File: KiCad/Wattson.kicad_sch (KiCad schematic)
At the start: 15 parts, among them J1 DC, J2 USB A, J3 Banana/Spade, J4 Banana/Spade, J5 USB A, J6 Spade/Banana/Alligator, J7 Spade/Banana/Alligator, M1 24V, SW1 Power On, U1 Power Monitor VIN, U2 Power Monitor VADJ, U3 LM317 Regulator (VADJ 4V5-40V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

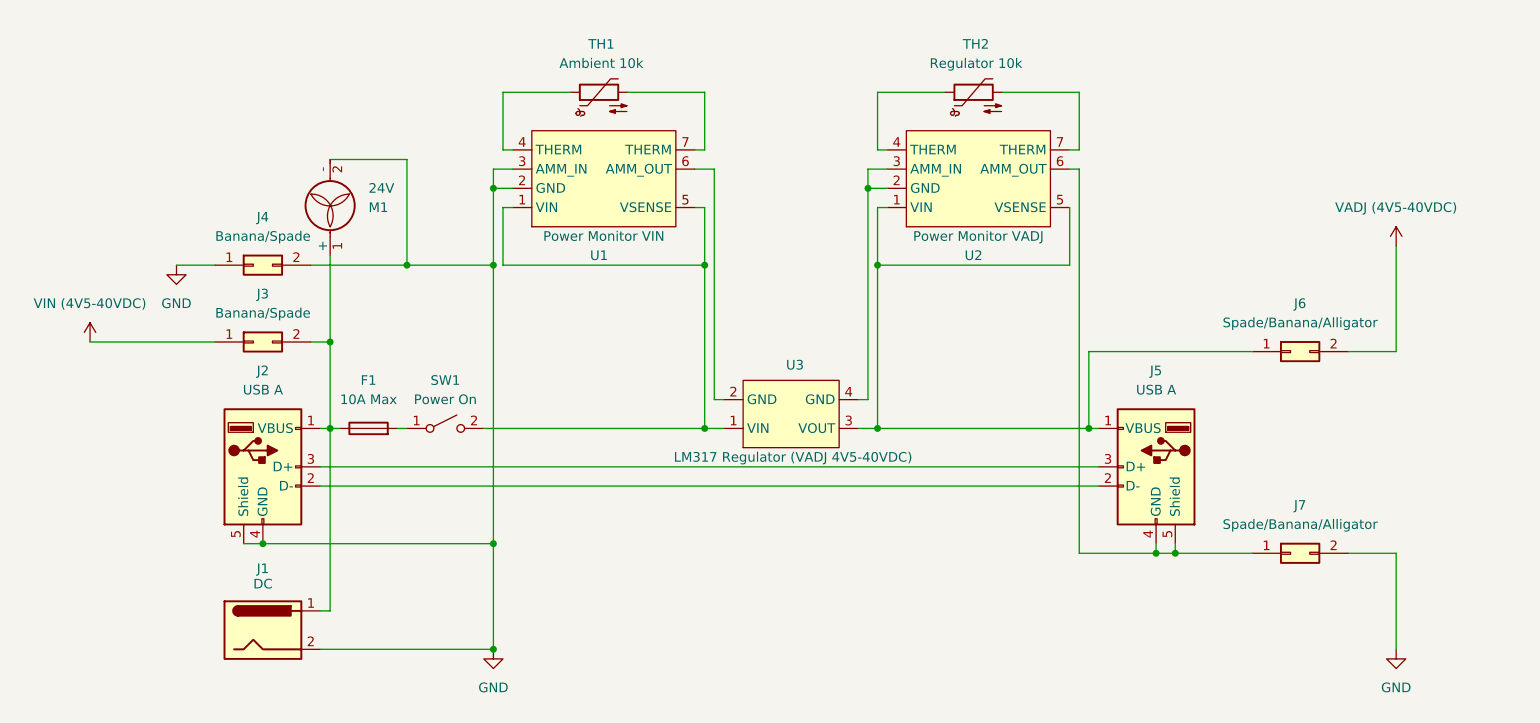
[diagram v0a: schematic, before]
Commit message: Vbus blocking diode
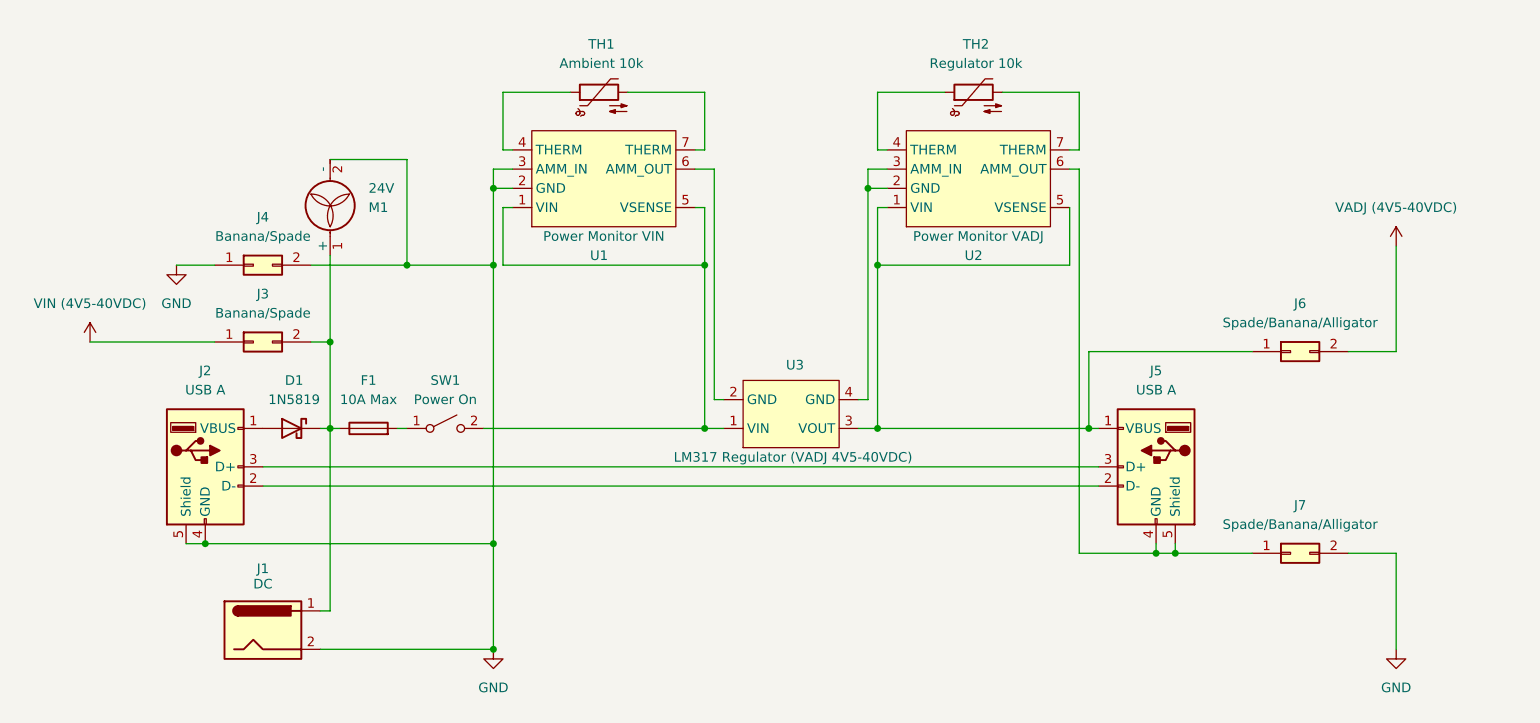
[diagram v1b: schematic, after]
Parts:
- added D1: 1N5819, Diode_THT:D_DO-41_SOD81_P10.16mm_Horizontal, symbol Diode:1N5819
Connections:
- net at F1.1, J1.1, J3.2 (Pin_2)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: now also D1.1 (K); no longer J2.1 (VBUS)
- new net: D1.2 (A), J2.1 (VBUS)
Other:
- moved on the sheet: J2
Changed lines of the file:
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@@
 	(title_block
 		(title "Wattson")
-		(date "2025-04-20")
-		(rev "1")
+		(date "2025-09-02")
+		(rev "1.1")
 		(company "Illusion Interactive")
 	)
@@
 	)
 	(junction
+		(at 60.96 125.73)
+		(diameter 0)
+		(color 0 0 0 0)
+	)
+	(junction
 		(at 99.06 139.7)
 		(diameter 0)
@@
 	)
 	(junction
-		(at 68.58 125.73)
-		(diameter 0)
-		(color 0 0 0 0)
-	)
-	(junction
 		(at 99.06 125.73)
 		(diameter 0)
@@
 	(wire
 		(pts
+			(xy 58.42 125.73) (xy 60.96 125.73)
+		)
+		(stroke
+			(width 0)
+			(type default)
+		)
+	)
+	(wire
+		(pts
 			(xy 148.59 78.74) (xy 151.13 78.74)
 		)
@@
 	(wire
 		(pts
-			(xy 68.58 125.73) (xy 99.06 125.73)
-		)
-		(stroke
-			(width 0)
-			(type default)
-		)
-	)
-	(wire
-		(pts
 			(xy 149.86 73.66) (xy 149.86 66.04)
 		)
@@
 	(wire
 		(pts
+			(xy 60.96 125.73) (xy 99.06 125.73)
+		)
+		(stroke
+			(width 0)
+			(type default)
+		)
+	)
+	(wire
+		(pts
 			(xy 77.47 74.93) (xy 87.63 74.93)
 		)
@@
 	(wire
 		(pts
-			(xy 77.47 110.49) (xy 76.2 110.49)
-		)
-		(stroke
-			(width 0)
-			(type default)
-		)
-	)
-	(wire
-		(pts
 			(xy 99.06 78.74) (xy 101.6 78.74)
 		)
@@
 	(wire
 		(pts
-			(xy 76.2 118.11) (xy 179.07 118.11)
+			(xy 68.58 118.11) (xy 179.07 118.11)
 		)
 		(stroke
@@
 	(wire
 		(pts
-			(xy 76.2 115.57) (xy 179.07 115.57)
+			(xy 68.58 115.57) (xy 179.07 115.57)
 		)
 		(stroke
@@
 	(wire
 		(pts
-			(xy 66.04 125.73) (xy 68.58 125.73)
+			(xy 76.2 110.49) (xy 77.47 110.49)
 		)
 		(stroke
@@
 	)
 	(symbol
+		(lib_id "Diode:1N5819")
+		(at 72.39 110.49 0)
+		(mirror y)
+		(unit 1)
+		(exclude_from_sim no)
+		(in_bom yes)
+		(on_board yes)
+		(dnp no)
+		(fields_autoplaced yes)
+		(property "Reference" "D1"
+			(at 72.7075 104.14 0)
+			(effects
+				(font
+					(size 1.27 1.27)
+				)
+			)
+		)
+		(property "Value" "1N5819"
+			(at 72.7075 106.68 0)
+			(effects
+				(font
+					(size 1.27 1.27)
+				)
+			)
+		)
+		(property "Footprint" "Diode_THT:D_DO-41_SOD81_P10.16mm_Horizontal"
+			(at 72.39 114.935 0)
+			(effects
+				(font
+					(size 1.27 1.27)
+				)
+				(hide yes)
+			)
+		)
+		(property "Datasheet" "http://www.vishay.com/docs/88525/1n5817.pdf"
+			(at 72.39 110.49 0)
+			(effects
+				(font
+					(size 1.27 1.27)
+				)
+				(hide yes)
+			)
+		)
+		(property "Description" "40V 1A Schottky Barrier Rectifier Diode, DO-41"
+			(at 72.39 110.49 0)
+			(effects
+				(font
+					(size 1.27 1.27)
+				)
+				(hide yes)
+			)
+		)
+		(pin "1"
+		)
+		(pin "2"
+		)
+		(instances
+			(project ""
+				(path "/9ec3a084-5570-4bec-a81d-dd13352c1d50"
+					(reference "D1")
+					(unit 1)
+				)
+			)
+		)
+	)
+	(symbol
 		(lib_id "power:GND")
 		(at 99.06 139.7 0)
@@
 	(symbol
 		(lib_id "Connector:USB_A")
-		(at 68.58 115.57 0)
+		(at 60.96 115.57 0)
 		(unit 1)
 		(exclude_from_sim no)
@@
 		(fields_autoplaced yes)
 		(property "Reference" "J2"
-			(at 68.58 102.87 0)
+			(at 60.96 102.87 0)
 			(effects
 				(font
@@
 		)
 		(property "Value" "USB A"
-			(at 68.58 105.41 0)
+			(at 60.96 105.41 0)
 			(effects
 				(font
@@
 		)
 		(property "Footprint" ""
-			(at 72.39 116.84 0)
+			(at 64.77 116.84 0)
 			(effects
 				(font
@@
 		)
 		(property "Datasheet" "~"
-			(at 72.39 116.84 0)
+			(at 64.77 116.84 0)
 			(effects
 				(font
@@
 		)
 		(property "Description" "USB Type A connector"
-			(at 68.58 115.57 0)
-			(effects
-				(font
+			(at 60.96 115.57 0)
+			(effects
+				(font

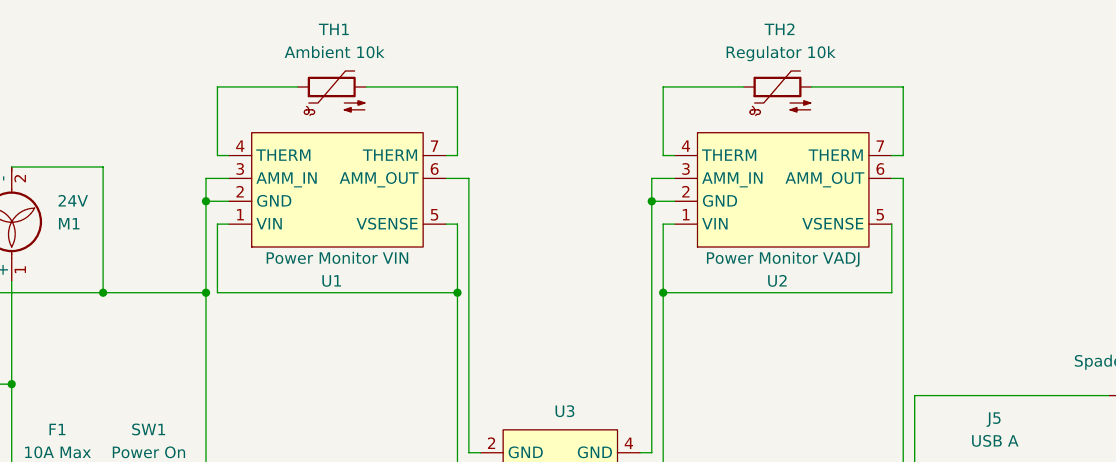
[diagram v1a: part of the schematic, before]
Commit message: Labels, readme update
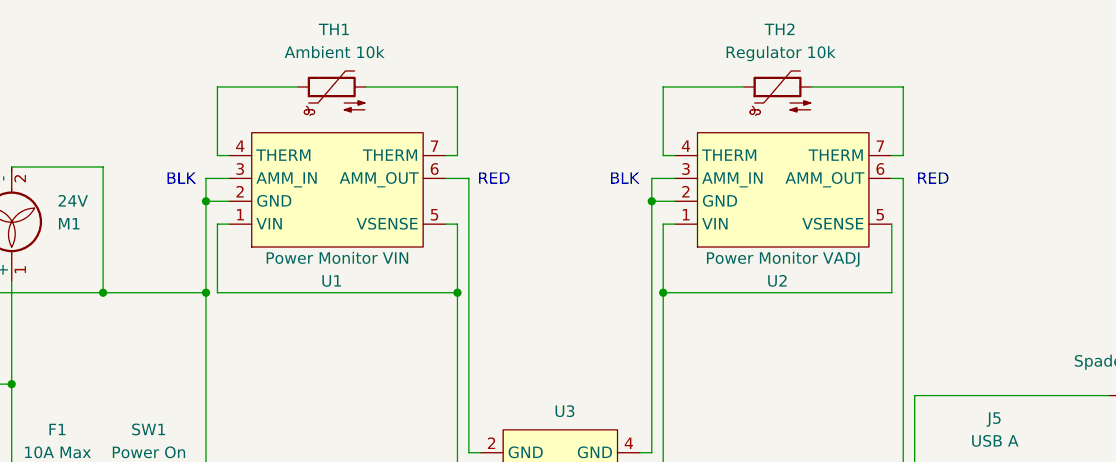
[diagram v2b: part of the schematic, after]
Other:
- note added: "BLK"
- note added: "RED"
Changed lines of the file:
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@@
 		(title "Wattson")
 		(date "2025-09-02")
-		(rev "1.1")
+		(rev "1.2")
 		(company "Illusion Interactive")
 	)
+	(text "BLK"
+		(exclude_from_sim no)
+		(at 145.542 76.454 0)
+		(effects
+			(font
+				(size 1.27 1.27)
+			)
+		)
+	)
+	(text "RED"
+		(exclude_from_sim no)
+		(at 179.832 76.454 0)
+		(effects
+			(font
+				(size 1.27 1.27)
+			)
+		)
+	)
+	(text "RED"
+		(exclude_from_sim no)
+		(at 131.064 76.454 0)
+		(effects
+			(font
+				(size 1.27 1.27)
+			)
+		)
+	)
+	(text "BLK"
+		(exclude_from_sim no)
+		(at 96.266 76.454 0)
+		(effects
+			(font
+				(size 1.27 1.27)
+			)
+		)
+	)
 	(junction

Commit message: Review
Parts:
- F1: value 10A Max -> 1A
- U3: value LM317 Regulator (VADJ 4V5-40VDC) -> LM317 Regulator (VADJ 5-22VDC)
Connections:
- net VADJ (4V5-40VDC) renamed VADJ (5-22VDC)
- net VIN (4V5-40VDC) renamed VIN (7-24VDC)
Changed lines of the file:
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@@
 	(title_block
 		(title "Wattson")
-		(date "2025-09-02")
-		(rev "1.2")
+		(date "2026-03-13")
+		(rev "1.3")
 		(company "Illusion Interactive")
 	)
@@
 			)
 		)
-		(property "Value" "10A Max"
+		(property "Value" "1A"
 			(at 82.55 106.68 90)
 			(effects
@@
 			)
 		)
-		(property "Value" "LM317 Regulator (VADJ 4V5-40VDC)"
+		(property "Value" "LM317 Regulator (VADJ 5-22VDC)"
 			(at 138.684 114.3 0)
 			(effects
@@
 		(on_board yes)
 		(dnp no)
-		(fields_autoplaced yes)
 		(property "Reference" "#PWR05"
 			(at 218.44 90.17 0)
@@
 			)
 		)
-		(property "Value" "VADJ (4V5-40VDC)"
-			(at 218.44 81.28 0)
-			(effects
-				(font
-					(size 1.27 1.27)
-				)
+		(property "Value" "VADJ (5-22VDC)"
+			(at 211.836 81.28 0)
+			(effects
+				(font
+					(size 1.27 1.27)
+				)
+				(justify left)
 			)
 		)
@@
 		(on_board yes)
 		(dnp no)
-		(fields_autoplaced yes)
 		(property "Reference" "#PWR02"
 			(at 45.72 102.87 0)
@@
 			)
 		)
-		(property "Value" "VIN (4V5-40VDC)"
-			(at 45.72 93.98 0)
-			(effects
-				(font
-					(size 1.27 1.27)
-				)
-			)
-		)
+		(property "Value" "VIN (7-24VDC)"
+			(at 38.608 94.488 0)
+			(effects
+				(font
+					(size 1.27 1.27)
+				)
+				(justify left)
+			)
+		)

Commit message: Update Wattson
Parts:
- J1: value DC -> DC (7-24VDC)
- U3: value LM317 Regulator (VADJ 5-22VDC) -> LM317 / LM350 / LM338 Regulator Module (VADJ 5-22VDC)
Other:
- note added: "16 AWG internal bus wiring."
- note added: "Optional"
- note added: "Sized for regulator."
- moved on the sheet: D1, F1, J1, J2, J3, J4, J5, J6, J7, M1, SW1, TH1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
